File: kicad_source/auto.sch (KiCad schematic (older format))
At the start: 11 parts

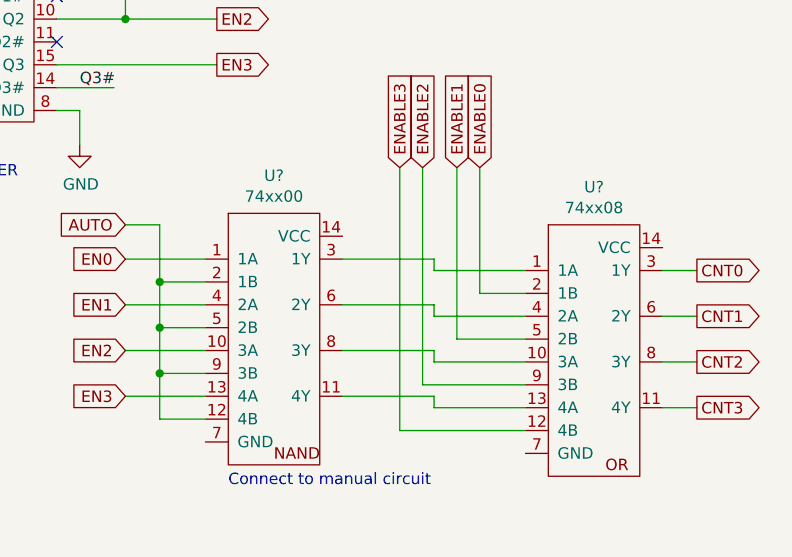
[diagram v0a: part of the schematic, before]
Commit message: added ground/ 3v3 connections
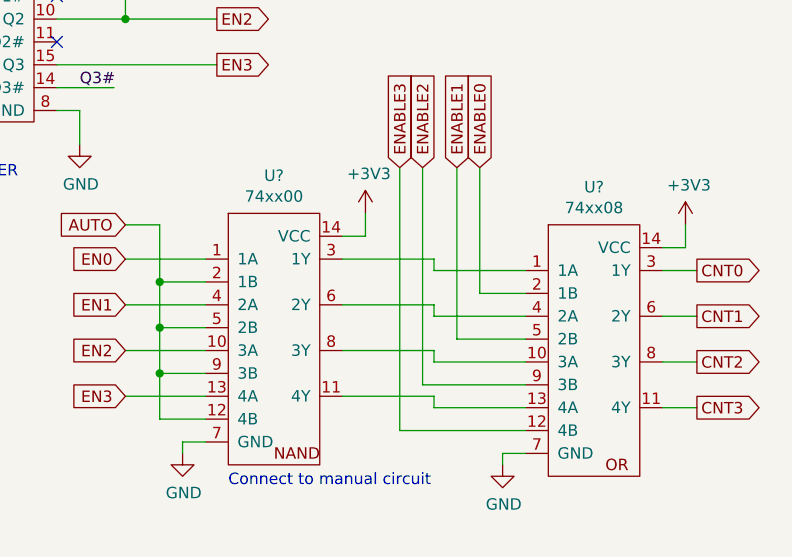
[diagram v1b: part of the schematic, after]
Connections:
- net +3V3: now also U?.14 (VCC), U?.14 (VCC)
- net GND: now also U?.7 (GND), U?.7 (GND)
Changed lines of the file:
@@
 Text Notes 8400 6400 0    50   ~ 0
 Connect to manual circuit
+$Comp
+L power-supply:+3V3 #PWR?
+U 1 1 5ED700EE
+P 9000 5200
+F 0 "#PWR?" H 9000 5050 50  0001 C CNN
+F 1 "+3V3" H 9015 5373 50  0000 C CNN
+F 2 "" H 9000 5200 50  0000 C CNN
+F 3 "" H 9000 5200 50  0000 C CNN
+	1    9000 5200
+	1    0    0    -1
+$EndComp
+$Comp
+L power-supply:+3V3 #PWR?
+U 1 1 5ED70610
+P 10400 5250
+F 0 "#PWR?" H 10400 5100 50  0001 C CNN
+F 1 "+3V3" H 10415 5423 50  0000 C CNN
+F 2 "" H 10400 5250 50  0000 C CNN
+F 3 "" H 10400 5250 50  0000 C CNN
+	1    10400 5250
+	1    0    0    -1
+$EndComp
+$Comp
+L power-supply:GND #PWR?
+U 1 1 5ED70A57
+P 9600 6300
+F 0 "#PWR?" H 9600 6050 50  0001 C CNN
+F 1 "GND" H 9605 6127 50  0000 C CNN
+F 2 "" H 9600 6300 50  0000 C CNN
+F 3 "" H 9600 6300 50  0000 C CNN
+	1    9600 6300
+	1    0    0    -1
+$EndComp
+$Comp
+L power-supply:GND #PWR?
+U 1 1 5ED70DE4
+P 8200 6250
+F 0 "#PWR?" H 8200 6000 50  0001 C CNN
+F 1 "GND" H 8205 6077 50  0000 C CNN
+F 2 "" H 8200 6250 50  0000 C CNN
+F 3 "" H 8200 6250 50  0000 C CNN
+	1    8200 6250
+	1    0    0    -1
+$EndComp
+Wire Wire Line
+	9700 6250 9600 6250
+Wire Wire Line
+	9600 6250 9600 6300
+Wire Wire Line
+	8200 6250 8200 6200
+Wire Wire Line
+	8200 6200 8300 6200
+Wire Wire Line
+	9000 5200 9000 5300
+Wire Wire Line
+	9000 5300 8900 5300
+Wire Wire Line
+	10300 5350 10400 5350
+Wire Wire Line
+	10400 5350 10400 5250
 $EndSCHEMATC

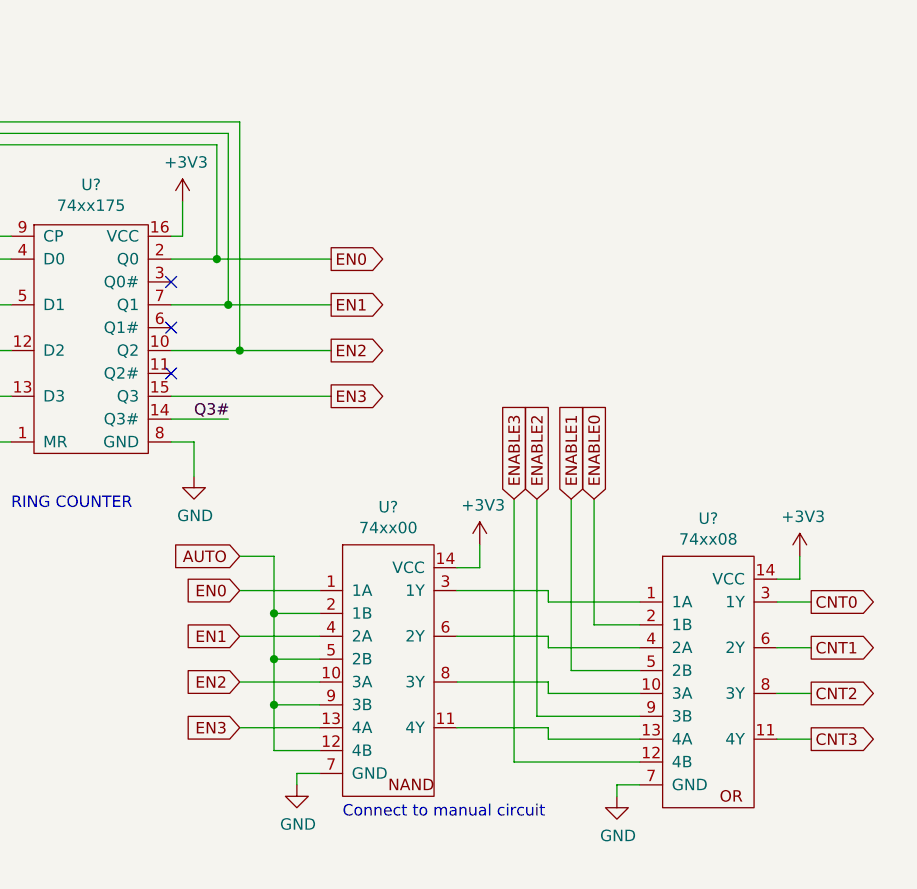
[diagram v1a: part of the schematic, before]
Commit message: changed and colorized logic table
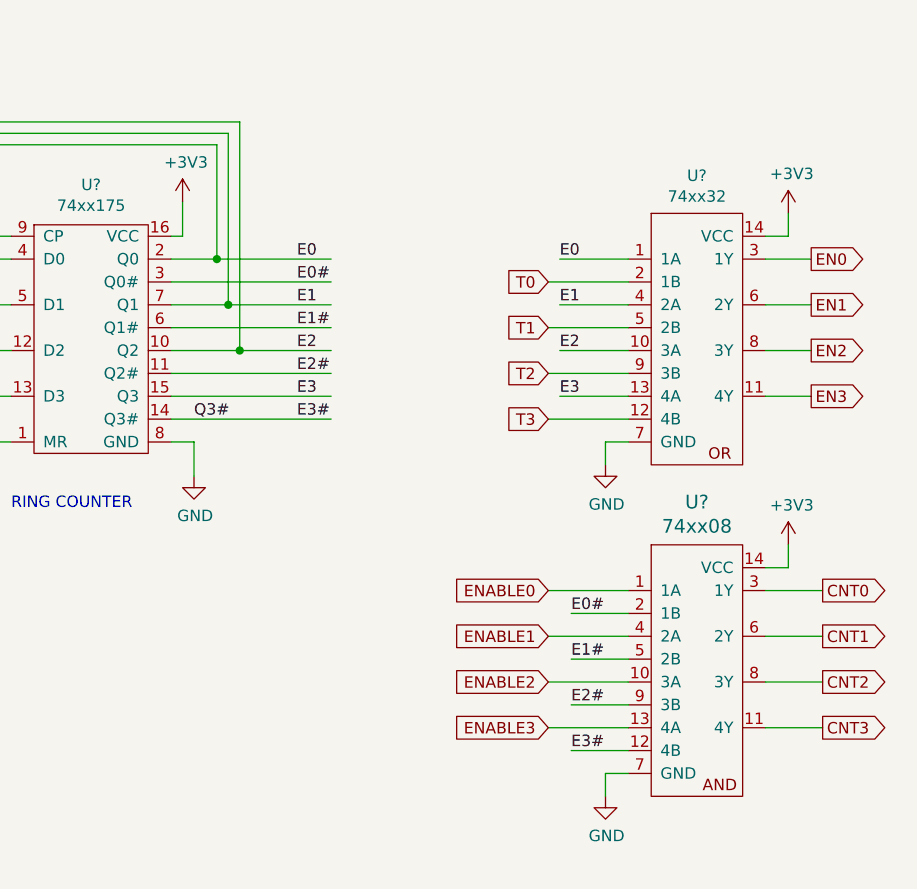
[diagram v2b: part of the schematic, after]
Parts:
- removed U?: 74xx08, symbol IC_logic:74xx32
- removed U?: 74xx00, symbol IC_logic:74xx00
- added U?: 74xx32, symbol IC_logic:74xx32
- added U?: 74xx08, SOIC:SOIC-14_3.9x8.7mm_Pitch1.27mm, symbol IC_logic:74xx08
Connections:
- net labels added: E0, E0#, E1, E1#, E2, E2#, E3, E3#, T0, T1, T2, T3
- wire segments 155 -> 145
- no-connect marks 10 -> 7
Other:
- note removed: "Connect to manual circuit"

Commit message: added connector for I2C, annotated schematic
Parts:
- gave numbers to parts that had none: 11
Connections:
- net labels added: I2C_INT
- wire segments 145 -> 146
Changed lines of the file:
@@
 P 3200 2150
 AR Path="/5EDEF6C9" Ref="U?"  Part="1"
-AR Path="/5EDDA6D0/5EDEF6C9" Ref="U?"  Part="1"
-F 0 "U?" H 3200 2675 50  0000 C CNN
+AR Path="/5EDDA6D0/5EDEF6C9" Ref="U14"  Part="1"
+F 0 "U14" H 3200 2675 50  0000 C CNN
 F 1 "NE555" H 3200 2584 50  0000 C CNN
 F 2 "" H 3200 2150 50  0001 C CNN
@@
 P 4000 1600
 AR Path="/5EDEF6CF" Ref="#PWR?"  Part="1"
-AR Path="/5EDDA6D0/5EDEF6CF" Ref="#PWR?"  Part="1"
-F 0 "#PWR?" H 4000 1450 50  0001 C CNN
+AR Path="/5EDDA6D0/5EDEF6CF" Ref="#PWR053"  Part="1"
+F 0 "#PWR053" H 4000 1450 50  0001 C CNN
 F 1 "+3V3" H 4015 1773 50  0000 C CNN
 F 2 "" H 4000 1600 50  0000 C CNN
@@
 P 3700 2750
 AR Path="/5EDEF6D5" Ref="#PWR?"  Part="1"
-AR Path="/5EDDA6D0/5EDEF6D5" Ref="#PWR?"  Part="1"
-F 0 "#PWR?" H 3700 2500 50  0001 C CNN
+AR Path="/5EDDA6D0/5EDEF6D5" Ref="#PWR052"  Part="1"
+F 0 "#PWR052" H 3700 2500 50  0001 C CNN
 F 1 "GND" H 3705 2577 50  0000 C CNN
 F 2 "" H 3700 2750 50  0000 C CNN
@@
 P 4000 1800
 AR Path="/5EDEF6DB" Ref="C?"  Part="1"
-AR Path="/5EDDA6D0/5EDEF6DB" Ref="C?"  Part="1"
-F 0 "C?" H 4092 1846 50  0000 L CNN
+AR Path="/5EDDA6D0/5EDEF6DB" Ref="C17"  Part="1"
+F 0 "C17" H 4092 1846 50  0000 L CNN
 F 1 "100nF" H 4092 1755 50  0000 L CNN
 F 2 "capacitors:C_0603" H 4000 1650 50  0001 C CNN
@@
 P 2450 2350
 AR Path="/5EDEF6E1" Ref="C?"  Part="1"
-AR Path="/5EDDA6D0/5EDEF6E1" Ref="C?"  Part="1"
-F 0 "C?" H 2542 2396 50  0000 L CNN
+AR Path="/5EDDA6D0/5EDEF6E1" Ref="C15"  Part="1"
+F 0 "C15" H 2542 2396 50  0000 L CNN
 F 1 "100nF" H 2542 2305 50  0000 L CNN
 F 2 "capacitors:C_0603" H 2450 2200 50  0001 C CNN
@@
 P 2450 2050
 AR Path="/5EDEF6E7" Ref="R?"  Part="1"
-AR Path="/5EDDA6D0/5EDEF6E7" Ref="R?"  Part="1"
-F 0 "R?" H 2509 2096 50  0000 L CNN
+AR Path="/5EDDA6D0/5EDEF6E7" Ref="R4"  Part="1"
+F 0 "R4" H 2509 2096 50  0000 L CNN
 F 1 "R_0603" H 2509 2005 50  0000 L CNN
 F 2 "resistors:R_0603" H 2450 1900 50  0001 C CNN
@@
 P 2450 1700
 AR Path="/5EDEF6ED" Ref="R?"  Part="1"
-AR Path="/5EDDA6D0/5EDEF6ED" Ref="R?"  Part="1"
-F 0 "R?" H 2509 1746 50  0000 L CNN
+AR Path="/5EDDA6D0/5EDEF6ED" Ref="R3"  Part="1"
+F 0 "R3" H 2509 1746 50  0000 L CNN
 F 1 "R_0603" H 2509 1655 50  0000 L CNN
 F 2 "resistors:R_0603" H 2450 1550 50  0001 C CNN
@@
 P 2450 1550
 AR Path="/5EDEF6F3" Ref="#PWR?"  Part="1"
-AR Path="/5EDDA6D0/5EDEF6F3" Ref="#PWR?"  Part="1"
-F 0 "#PWR?" H 2450 1400 50  0001 C CNN
+AR Path="/5EDDA6D0/5EDEF6F3" Ref="#PWR048"  Part="1"
+F 0 "#PWR048" H 2450 1400 50  0001 C CNN
 F 1 "+3V3" H 2465 1723 50  0000 C CNN
 F 2 "" H 2450 1550 50  0000 C CNN
@@
 P 2450 2550
 AR Path="/5EDEF6F9" Ref="#PWR?"  Part="1"
-AR Path="/5EDDA6D0/5EDEF6F9" Ref="#PWR?"  Part="1"
-F 0 "#PWR?" H 2450 2300 50  0001 C CNN
+AR Path="/5EDDA6D0/5EDEF6F9" Ref="#PWR049"  Part="1"
+F 0 "#PWR049" H 2450 2300 50  0001 C CNN
 F 1 "GND" H 2455 2377 50  0000 C CNN
 F 2 "" H 2450 2550 50  0000 C CNN
@@
 P 4000 1950
 AR Path="/5EDEF6FF" Ref="#PWR?"  Part="1"
-AR Path="/5EDDA6D0/5EDEF6FF" Ref="#PWR?"  Part="1"
-F 0 "#PWR?" H 4000 1700 50  0001 C CNN
+AR Path="/5EDDA6D0/5EDEF6FF" Ref="#PWR054"  Part="1"
+F 0 "#PWR054" H 4000 1700 50  0001 C CNN
 F 1 "GND" H 4005 1777 50  0000 C CNN
 F 2 "" H 4000 1950 50  0000 C CNN
@@
 P 3700 2600
 AR Path="/5EDEF705" Ref="C?"  Part="1"
-AR Path="/5EDDA6D0/5EDEF705" Ref="C?"  Part="1"
-F 0 "C?" H 3792 2646 50  0000 L CNN
+AR Path="/5EDDA6D0/5EDEF705" Ref="C16"  Part="1"
+F 0 "C16" H 3792 2646 50  0000 L CNN
 F 1 "100nF" H 3792 2555 50  0000 L CNN
 F 2 "capacitors:C_0603" H 3700 2450 50  0001 C CNN
@@
 P 7300 4300
 AR Path="/5EDF7AF9" Ref="U?"  Part="1"
-AR Path="/5EDDA6D0/5EDF7AF9" Ref="U?"  Part="1"
-F 0 "U?" H 7300 4975 50  0000 C CNN
+AR Path="/5EDDA6D0/5EDF7AF9" Ref="U17"  Part="1"
+F 0 "U17" H 7300 4975 50  0000 C CNN
 F 1 "74xx175" H 7300 4884 50  0000 C CNN
 F 2 "" H 7300 4300 50  0001 C CNN
@@
 P 3650 5500
 AR Path="/5EE42B61" Ref="U?"  Part="1"
-AR Path="/5EDDA6D0/5EE42B61" Ref="U?"  Part="1"
-F 0 "U?" H 3650 6175 50  0000 C CNN
+AR Path="/5EDDA6D0/5EE42B61" Ref="U15"  Part="1"
+F 0 "U15" H 3650 6175 50  0000 C CNN
 F 1 "74xx175" H 3650 6084 50  0000 C CNN
 F 2 "" H 3650 5500 50  0001 C CNN
@@
 P 5050 4300
 AR Path="/5EE54782" Ref="U?"  Part="1"
-AR Path="/5EDDA6D0/5EE54782" Ref="U?"  Part="1"
-F 0 "U?" H 5050 5065 50  0000 C CNN
+AR Path="/5EDDA6D0/5EE54782" Ref="U16"  Part="1"
+F 0 "U16" H 5050 5065 50  0000 C CNN
 F 1 "74xx00" H 5050 4974 50  0000 C CNN
 F 2 "SOIC:SOIC-14_3.9x8.7mm_Pitch1.27mm" H 5050 4300 50  0001 C CNN
@@
 	7750 4750 7750 4900
 $Comp
-L power-supply:+3V3 #PWR?
+L power-supply:+3V3 #PWR058
 U 1 1 5EF7310C
 P 7700 3700
-F 0 "#PWR?" H 7700 3550 50  0001 C CNN
+F 0 "#PWR058" H 7700 3550 50  0001 C CNN
 F 1 "+3V3" H 7715 3873 50  0000 C CNN
 F 2 "" H 7700 3700 50  0000 C CNN
@@
 $EndComp
 $Comp
-L power-supply:+3V3 #PWR?
+L power-supply:+3V3 #PWR055
 U 1 1 5EF735CB
 P 4150 4750
-F 0 "#PWR?" H 4150 4600 50  0001 C CNN
+F 0 "#PWR055" H 4150 4600 50  0001 C CNN
 F 1 "+3V3" H 4165 4923 50  0000 C CNN
 F 2 "" H 4150 4750 50  0000 C CNN
@@
 $EndComp
 $Comp
-L power-supply:+3V3 #PWR?
+L power-supply:+3V3 #PWR057
 U 1 1 5EF73974
 P 5500 3600
-F 0 "#PWR?" H 5500 3450 50  0001 C CNN
+F 0 "#PWR057" H 5500 3450 50  0001 C CNN
 F 1 "+3V3" H 5515 3773 50  0000 C CNN
 F 2 "" H 5500 3600 50  0000 C CNN
@@
 	7700 3850 7650 3850
 $Comp
-L power-supply:+3V3 #PWR?
+L power-supply:+3V3 #PWR050
 U 1 1 5EF87C74
 P 2900 5800
-F 0 "#PWR?" H 2900 5650 50  0001 C CNN
+F 0 "#PWR050" H 2900 5650 50  0001 C CNN
 F 1 "+3V3" H 2915 5973 50  0000 C CNN
 F 2 "" H 2900 5800 50  0000 C CNN
@@
 $EndComp
 $Comp
-L power-supply:GND #PWR?
+L power-supply:GND #PWR051
 U 1 1 5EF883E0
 P 3200 6400
-F 0 "#PWR?" H 3200 6150 50  0001 C CNN
+F 0 "#PWR051" H 3200 6150 50  0001 C CNN
 F 1 "GND" H 3205 6227 50  0000 C CNN
 F 2 "" H 3200 6400 50  0000 C CNN
@@
 $EndComp
 $Comp
-L power-supply:GND #PWR?
+L power-supply:GND #PWR056
 U 1 1 5EF89116
 P 4600 4900
-F 0 "#PWR?" H 4600 4650 50  0001 C CNN
+F 0 "#PWR056" H 4600 4650 50  0001 C CNN
 F 1 "GND" H 4605 4727 50  0000 C CNN
 F 2 "" H 4600 4900 50  0000 C CNN
@@
 $EndComp
 $Comp
-L power-supply:GND #PWR?
+L power-supply:GND #PWR059
 U 1 1 5EF8958A
 P 7750 4900
-F 0 "#PWR?" H 7750 4650 50  0001 C CNN
+F 0 "#PWR059" H 7750 4650 50  0001 C CNN
 F 1 "GND" H 7755 4727 50  0000 C CNN
 F 2 "" H 7750 4900 50  0000 C CNN
@@
 E3#
 $Comp
-L IC_logic:74xx32 U?
+L IC_logic:74xx32 U19
 U 1 1 5EF4E33D
 P 9900 4850
-F 0 "U?" H 9950 6115 50  0000 C CNN
+F 0 "U19" H 9950 6115 50  0000 C CNN
 F 1 "74xx32" H 9950 6024 50  0000 C CNN
 F 2 "" H 9900 4850 50  0001 C CNN
@@
 E3
 $Comp
-L IC_logic:74xx08 U?
+L IC_logic:74xx08 U18
 U 1 1 5EF82717
 P 9750 5700
-F 0 "U?" H 9950 6387 60  0000 C CNN
+F 0 "U18" H 9950 6387 60  0000 C CNN
 F 1 "74xx08" H 9950 6281 60  0000 C CNN
 F 2 "SOIC:SOIC-14_3.9x8.7mm_Pitch1.27mm" H 10050 5550 60  0001 C CNN
@@
 	9550 6200 9550 6300
 $Comp
-L power-supply:+3V3 #PWR?
+L power-supply:+3V3 #PWR062
 U 1 1 5EFF69D6
 P 10350 3750
-F 0 "#PWR?" H 10350 3600 50  0001 C CNN
+F 0 "#PWR062" H 10350 3600 50  0001 C CNN
 F 1 "+3V3" H 10365 3923 50  0000 C CNN
 F 2 "" H 10350 3750 50  0000 C CNN
@@
 $EndComp
 $Comp
-L power-supply:GND #PWR?
+L power-supply:GND #PWR060
 U 1 1 5EFF6F21
 P 9550 4850
-F 0 "#PWR?" H 9550 4600 50  0001 C CNN
+F 0 "#PWR060" H 9550 4600 50  0001 C CNN
 F 1 "GND" H 9555 4677 50  0000 C CNN
 F 2 "" H 9550 4850 50  0000 C CNN
@@
 $EndComp
 $Comp
-L power-supply:+3V3 #PWR?
+L power-supply:+3V3 #PWR063
 U 1 1 5EFF73E0
 P 10350 5200
-F 0 "#PWR?" H 10350 5050 50  0001 C CNN
+F 0 "#PWR063" H 10350 5050 50  0001 C CNN
 F 1 "+3V3" H 10365 5373 50  0000 C CNN
 F 2 "" H 10350 5200 50  0000 C CNN
@@
 $EndComp
 $Comp
-L power-supply:GND #PWR?
+L power-supply:GND #PWR061
 U 1 1 5EFF7A2D
 P 9550 6300
-F 0 "#PWR?" H 9550 6050 50  0001 C CNN
+F 0 "#PWR061" H 9550 6050 50  0001 C CNN
 F 1 "GND" H 9555 6127 50  0000 C CNN
 F 2 "" H 9550 6300 50  0000 C CNN
@@
 	1    0    0    -1
 $EndComp
+Text GLabel 7000 5500 2    50   Output ~ 0
+I2C_INT
+Wire Wire Line
+	6250 5500 7000 5500
+Text Label 6400 5500 0    50   ~ 0
+I2C_INT
 $EndSCHEMATC

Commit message: exchanged I2C expanders to TCA9535 (16 bit type), generated schematic pdf
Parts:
- U14: footprint (none) -> SOIC:SOIC-8_3.9x4.9mm_Pitch1.27mm; symbol SonarExtenderI2C-rescue:NE555-IC_logic -> IC_logic:NE555
- U15, U17: footprint (none) -> SOIC:SOIC-16_3.9x9.9mm_Pitch1.27mm; symbol SonarExtenderI2C-rescue:74xx175-IC_logic -> IC_logic:74xx175
- U16: symbol SonarExtenderI2C-rescue:74xx00-IC_logic -> IC_logic:74xx00
- U19: footprint (none) -> SOIC:SOIC-14_3.9x8.7mm_Pitch1.27mm
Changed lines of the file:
@@
 $EndDescr
 $Comp
-L SonarExtenderI2C-rescue:NE555-IC_logic U?
+L IC_logic:NE555 U?
 U 1 1 5EDEF6C9
 P 3200 2150
@@
 F 0 "U14" H 3200 2675 50  0000 C CNN
 F 1 "NE555" H 3200 2584 50  0000 C CNN
-F 2 "" H 3200 2150 50  0001 C CNN
+F 2 "SOIC:SOIC-8_3.9x4.9mm_Pitch1.27mm" H 3200 2150 50  0001 C CNN
 F 3 "" H 3200 2150 50  0001 C CNN
 	1    3200 2150
@@
 CLK_10Hz
 $Comp
-L SonarExtenderI2C-rescue:74xx175-IC_logic U?
+L IC_logic:74xx175 U?
 U 1 1 5EDF7AF9
 P 7300 4300
@@
 F 0 "U17" H 7300 4975 50  0000 C CNN
 F 1 "74xx175" H 7300 4884 50  0000 C CNN
-F 2 "" H 7300 4300 50  0001 C CNN
+F 2 "SOIC:SOIC-16_3.9x9.9mm_Pitch1.27mm" H 7300 4300 50  0001 C CNN
 F 3 "" H 7300 4300 50  0001 C CNN
 	1    7300 4300
@@
 	7650 4550 8350 4550
 $Comp
-L SonarExtenderI2C-rescue:74xx175-IC_logic U?
+L IC_logic:74xx175 U?
 U 1 1 5EE42B61
 P 3650 5500
@@
 F 0 "U15" H 3650 6175 50  0000 C CNN
 F 1 "74xx175" H 3650 6084 50  0000 C CNN
-F 2 "" H 3650 5500 50  0001 C CNN
+F 2 "SOIC:SOIC-16_3.9x9.9mm_Pitch1.27mm" H 3650 5500 50  0001 C CNN
 F 3 "" H 3650 5500 50  0001 C CNN
 	1    3650 5500
@@
 $EndComp
 $Comp
-L SonarExtenderI2C-rescue:74xx00-IC_logic U?
+L IC_logic:74xx00 U?
 U 1 1 5EE54782
-P 5050 4300
+P 5050 4700
 AR Path="/5EE54782" Ref="U?"  Part="1"
 AR Path="/5EDDA6D0/5EE54782" Ref="U16"  Part="1"
-F 0 "U16" H 5050 5065 50  0000 C CNN
-F 1 "74xx00" H 5050 4974 50  0000 C CNN
-F 2 "SOIC:SOIC-14_3.9x8.7mm_Pitch1.27mm" H 5050 4300 50  0001 C CNN
-F 3 "" H 5050 4300 50  0001 C CNN
-	1    5050 4300
+F 0 "U16" H 5050 5465 50  0000 C CNN
+F 1 "74xx00" H 5050 5374 50  0000 C CNN
+F 2 "SOIC:SOIC-14_3.9x8.7mm_Pitch1.27mm" H 5050 4700 50  0001 C CNN
+F 3 "" H 5050 4700 50  0001 C CNN
+	1    5050 4700
 	1    0    0    -1
 $EndComp
@@
 F 0 "U19" H 9950 6115 50  0000 C CNN
 F 1 "74xx32" H 9950 6024 50  0000 C CNN
-F 2 "" H 9900 4850 50  0001 C CNN
+F 2 "SOIC:SOIC-14_3.9x8.7mm_Pitch1.27mm" H 9900 4850 50  0001 C CNN
 F 3 "" H 9900 4850 50  0001 C CNN
 	1    9900 4850
